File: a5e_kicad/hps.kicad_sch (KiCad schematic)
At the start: 3 parts, among them J8 Micro_SD_Card, U7 A5EB013B-B23B

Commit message: savegame
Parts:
- added U13: (no value), Package_BGA:Texas_YFP0020_DSBGA-20_1.588x1.988mm_Layout4x5_P0.4mm, symbol agilex_5_lib:TXS0206A
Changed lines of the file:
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@@
+	)
+	(symbol
+		(lib_id "agilex_5_lib:TXS0206A")
+		(at 62.23 158.75 0)
+		(unit 1)
+		(body_style 1)
+		(exclude_from_sim no)
+		(in_bom yes)
+		(on_board yes)
+		(in_pos_files yes)
+		(dnp no)
+		(fields_autoplaced yes)
+		(property "Reference" "U13"
+			(at 71.9933 140.97 0)
+			(show_name no)
+			(do_not_autoplace no)
+			(effects
+				(font
+					(size 1.27 1.27)
+				)
+				(justify left)
+			)
+		)
+		(property "Value" ""
+			(at 62.23 158.75 0)
+			(show_name no)
+			(do_not_autoplace no)
+			(effects
+				(font
+					(size 1.27 1.27)
+				)
+			)
+		)
+		(property "Footprint" "Package_BGA:Texas_YFP0020_DSBGA-20_1.588x1.988mm_Layout4x5_P0.4mm"
+			(at 62.23 158.75 0)
+			(hide yes)
+			(show_name no)
+			(do_not_autoplace no)
+			(effects
+				(font
+					(size 1.27 1.27)
+				)
+			)
+		)
+		(property "Datasheet" ""
+			(at 62.23 158.75 0)
+			(hide yes)
+			(show_name no)
+			(do_not_autoplace no)
+			(effects
+				(font
+					(size 1.27 1.27)
+				)
+			)
+		)
+		(property "Description" ""
+			(at 62.23 158.75 0)
+			(hide yes)
+			(show_name no)
+			(do_not_autoplace no)
+			(effects
+				(font
+					(size 1.27 1.27)
+				)
+			)
+		)
+		(pin "A3"
+		)
+		(pin "A2"
+		)
+		(pin "A1"
+		)
+		(pin "B4"
+		)
+		(pin "C4"
+		)
+		(pin "C3"
+		)
+		(pin "D1"
+		)
+		(pin "D3"
+		)
+		(pin "E1"
+		)
+		(pin "E2"
+		)
+		(pin "A4"
+		)
+		(pin "B3"
+		)
+		(pin "B1"
+		)
+		(pin "C1"
+		)
+		(pin "D4"
+		)
+		(pin "D2"
+		)
+		(pin "C2"
+		)
+		(pin "E4"
+		)
+		(instances
+			(project "agilex_3_soc"
+				(path "/a5b98d95-6877-4284-904f-d04e32723ae0/1bba180f-a717-40d4-b2d6-e5a7b998021f"
+					(reference "U13")
+					(unit 1)
+				)
+			)
+		)
 	)
 	(symbol

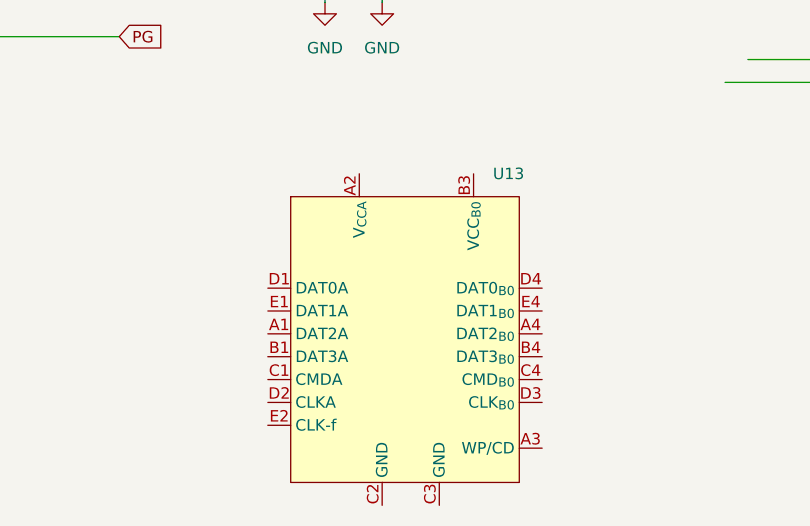
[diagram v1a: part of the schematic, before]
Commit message: choose clock ic:s
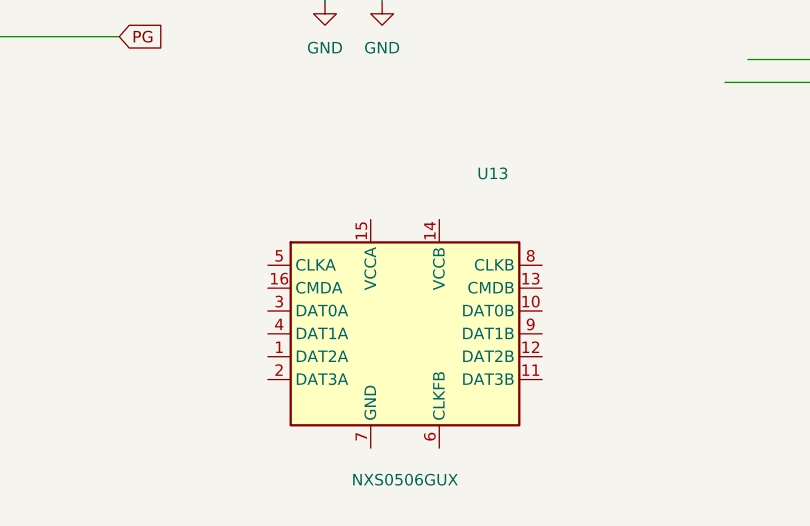
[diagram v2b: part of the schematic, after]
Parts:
- U13: value (none) -> NXS0506GUX; footprint Package_BGA:Texas_YFP0020_DSBGA-20_1.588x1.988mm_Layout4x5_P0.4mm -> agilex_lib:NXS0506GU_XQFN16_1.8x2.6mm_P0.4mm; symbol agilex_5_lib:TXS0206A -> agilex_5_lib:NXS0506GU
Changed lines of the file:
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@@
 	)
 	(symbol
-		(lib_id "agilex_5_lib:TXS0206A")
+		(lib_id "agilex_5_lib:NXS0506GU")
 		(at 62.23 158.75 0)
 		(unit 1)
@@
 					(size 1.27 1.27)
 				)
-				(justify left)
 			)
 		)
-		(property "Value" ""
-			(at 62.23 158.75 0)
+		(property "Value" "NXS0506GUX"
+			(at 62.23 175 0)
 			(show_name no)
 			(do_not_autoplace no)
@@
 			)
 		)
-		(property "Footprint" "Package_BGA:Texas_YFP0020_DSBGA-20_1.588x1.988mm_Layout4x5_P0.4mm"
+		(property "Footprint" "agilex_lib:NXS0506GU_XQFN16_1.8x2.6mm_P0.4mm"
 			(at 62.23 158.75 0)
 			(hide yes)
@@
 			)
 		)
-		(property "Datasheet" ""
+		(property "Datasheet" "https://assets.nexperia.com/documents/data-sheet/NXS0506.pdf"
 			(at 62.23 158.75 0)
 			(hide yes)
@@
 			)
 		)
-		(property "Description" ""
+		(property "Description" "SD 3.0 auto-direction 6-channel dual-supply level translator (CLK+CMD+DAT0-3), XQFN16 - no CD/WP passthrough"
 			(at 62.23 158.75 0)
 			(hide yes)
@@
 			)
 		)
-		(pin "A3"
+		(pin "1"
 		)
-		(pin "A2"
+		(pin "2"
 		)
-		(pin "A1"
+		(pin "3"
 		)
-		(pin "B4"
+		(pin "4"
 		)
-		(pin "C4"
+		(pin "5"
 		)
-		(pin "C3"
+		(pin "6"
 		)
-		(pin "D1"
+		(pin "7"
 		)
-		(pin "D3"
+		(pin "8"
 		)
-		(pin "E1"
+		(pin "9"
 		)
-		(pin "E2"
+		(pin "10"
 		)
-		(pin "A4"
+		(pin "11"
 		)
-		(pin "B3"
+		(pin "12"
 		)
-		(pin "B1"
+		(pin "13"
 		)
-		(pin "C1"
+		(pin "14"
 		)
-		(pin "D4"
+		(pin "15"
 		)
-		(pin "D2"
-		)
-		(pin "C2"
-		)
-		(pin "E4"
+		(pin "16"
 		)
 		(instances
